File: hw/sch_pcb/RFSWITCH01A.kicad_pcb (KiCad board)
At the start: 2 copper layers, 40.1 x 40.1 mm, 45 parts, among them J1 HEADER_2x03_PARALLEL, J10 HEADER_2x01_PARALLEL, J2 SMA, J3 SMA, J4 HEADER_2x01_PARALLEL, J5 HEADER_2x01_PARALLEL, J6 HEADER_2x01_PARALLEL, J7 SMA, J8 SMA, J9 HEADER_2x01_PARALLEL, M1 HOLE, M2 HOLE, M3 HOLE, M4 HOLE, U1 TPS22945DCKR, U2 PE4259, U3 SPF5189Z, U4 PE4259

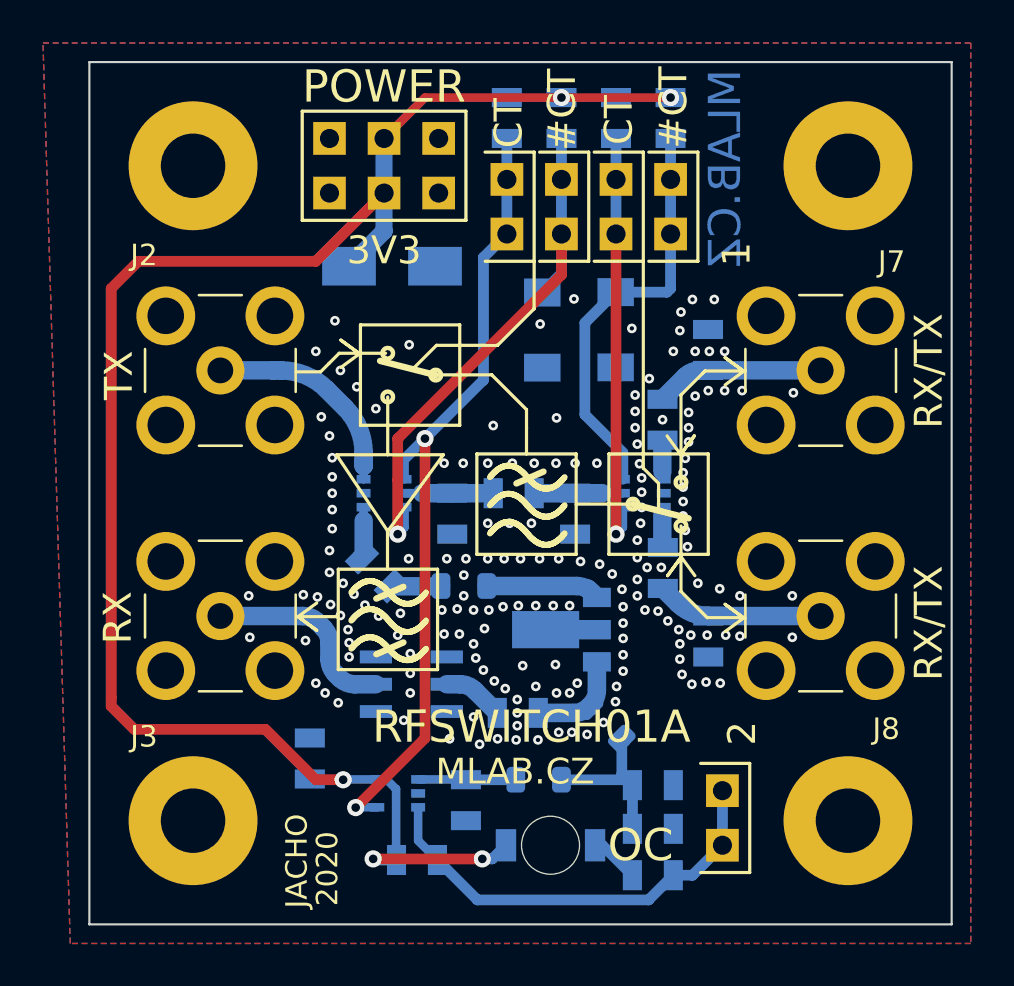
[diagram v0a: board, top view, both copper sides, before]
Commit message: Add shielding vias.
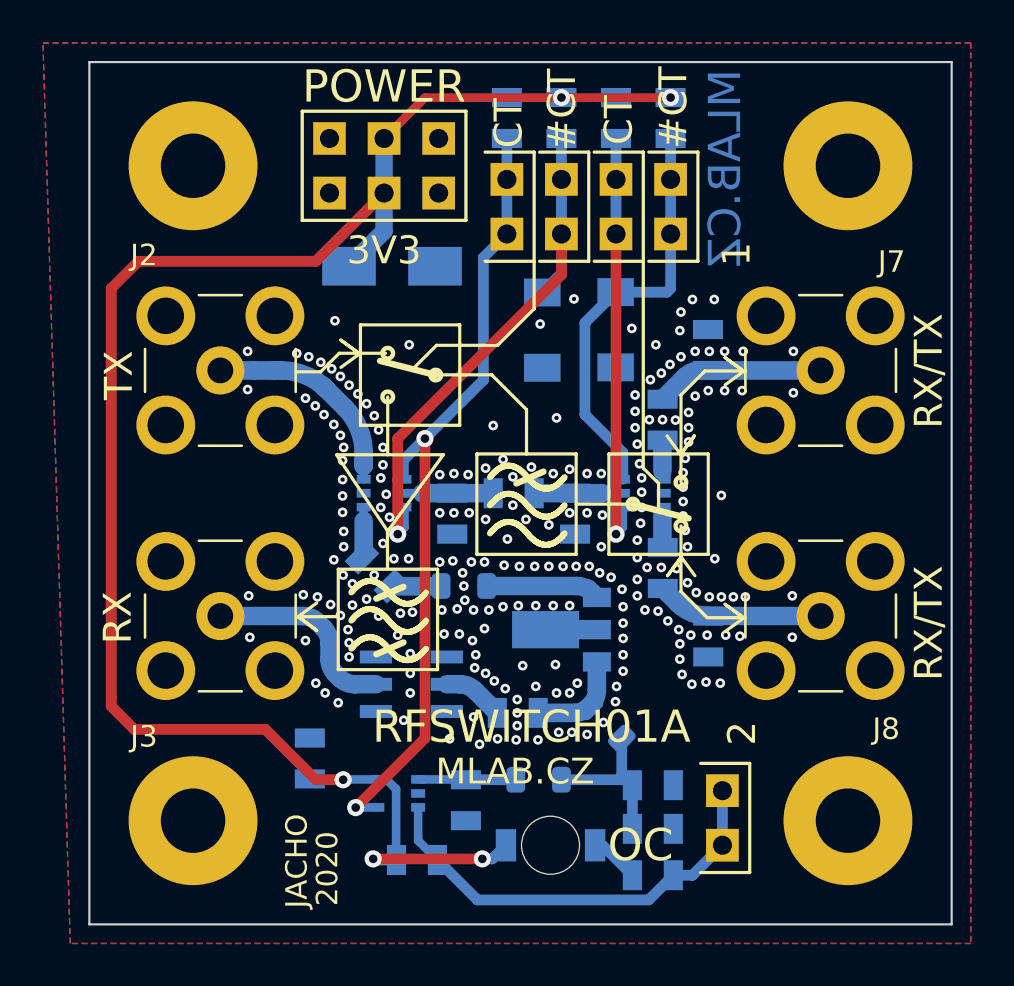
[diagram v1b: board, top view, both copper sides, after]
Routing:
- net GND: vias 170 -> 222
- net /SW1_#CTRL: vias 1 -> 2

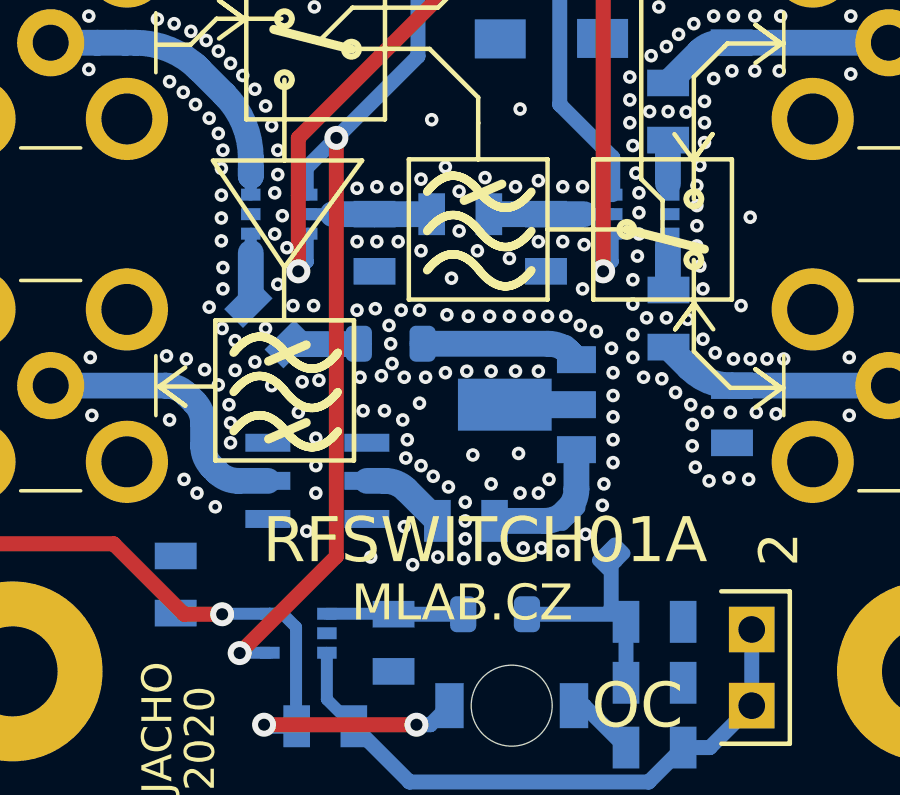
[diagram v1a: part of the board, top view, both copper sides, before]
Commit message: Fix DRC errors.
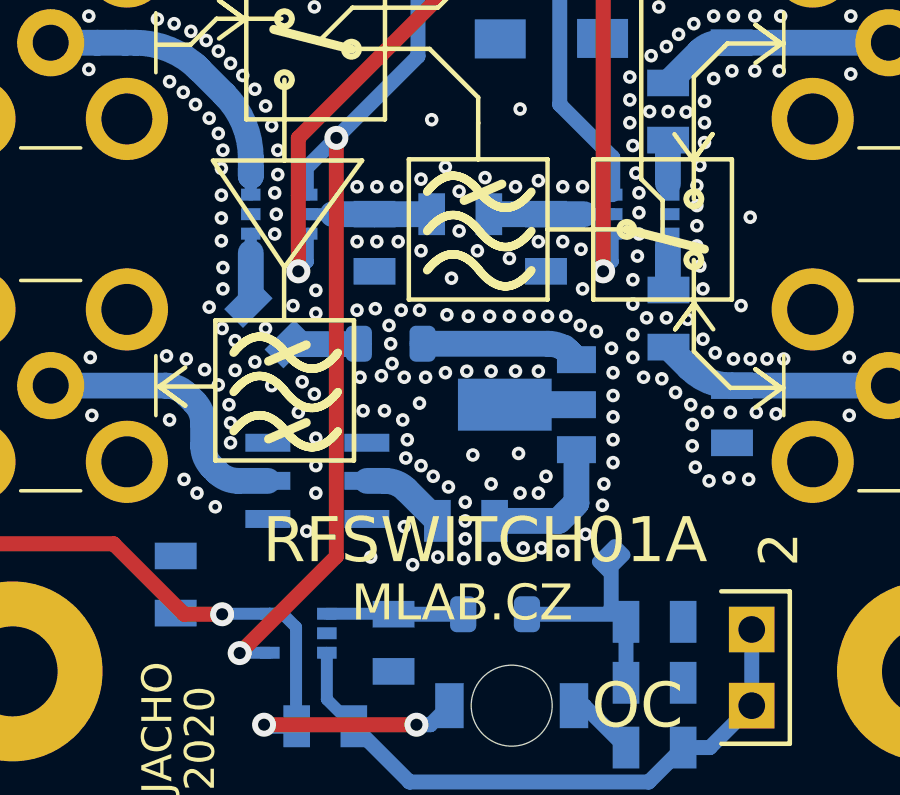
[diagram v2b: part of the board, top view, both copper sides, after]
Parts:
- moved L2 0.05 mm to (24.3, -9.60)
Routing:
- net /SW1_#CTRL: vias 2 -> 1
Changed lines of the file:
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@@
       (viasonmask false)
       (mode 1)
-      (useauxorigin false)
+      (useauxorigin true)
       (hpglpennumber 1)
       (hpglpenspeed 20)
@@
   )
   (module "Inductor_SMD:L_0805_2012Metric" (layer "B.Cu")
-    (at 24.2824 -9.652 135)
+    (at 24.2824 -9.598492 135)
     (descr "Inductor SMD 0805 (2012 Metric), square (rectangular) end terminal, IPC_7351 nominal, (Body size source: IPC-SM-782 page 80, https://www.pcb-3d.com/wordpress/wp-content/uploads/ipc-sm-782a_amendment_1_and_2.pdf), generated with kicad-footprint-generator")
     (tags "inductor")
@@
   (segment (start 13.97 -32.516027) (end 12.3383 -30.884327) (width 0.8) (layer "B.Cu") (net 1))
   (via (at 21.9964 -23.8252) (size 0.45) (drill 0.2) (layers "F.Cu" "B.Cu") (net 2))
-  (via (at 13.9192 -17.9832) (size 0.45) (drill 0.2) (layers "F.Cu" "B.Cu") (net 2))
+  (via (at 15.1892 -17.78) (size 0.45) (drill 0.2) (layers "F.Cu" "B.Cu") (net 2))
   (via (at 25.7556 -18.1356) (size 0.45) (drill 0.2) (layers "F.Cu" "B.Cu") (net 2))
   (via (at 28.2448 -13.716) (size 0.45) (drill 0.2) (layers "F.Cu" "B.Cu") (net 2))
   (via (at 20.1676 -10.0965) (size 0.45) (drill 0.2) (layers "F.Cu" "B.Cu") (net 2))
-  (via (at 15.2908 -14.7828) (size 0.45) (drill 0.2) (layers "F.Cu" "B.Cu") (net 2))
+  (via (at 15.1384 -14.3256) (size 0.45) (drill 0.2) (layers "F.Cu" "B.Cu") (net 2))
   (via (at 23.4188 -21.2344) (size 0.45) (drill 0.2) (layers "F.Cu" "B.Cu") (net 2))
   (via (at 13.8176 -21.0312) (size 0.45) (drill 0.2) (layers "F.Cu" "B.Cu") (net 2))
@@
   (via (at 28.956 -11.5316) (size 0.45) (drill 0.2) (layers "F.Cu" "B.Cu") (net 2))
   (via (at 18.1864 -12.192) (size 0.45) (drill 0.2) (layers "F.Cu" "B.Cu") (net 2))
-  (via (at 24.13 -19.304) (size 0.45) (drill 0.2) (layers "F.Cu" "B.Cu") (net 2))
+  (via (at 24.0284 -19.1516) (size 0.45) (drill 0.2) (layers "F.Cu" "B.Cu") (net 2))
   (via (at 29.1084 -15.494) (size 0.45) (drill 0.2) (layers "F.Cu" "B.Cu") (net 2))
   (via (at 26.929992 -23.741671) (size 0.45) (drill 0.2) (layers "F.Cu" "B.Cu") (net 2))
@@
   (via (at 28.0924 -17.8308) (size 0.45) (drill 0.2) (layers "F.Cu" "B.Cu") (net 2))
   (via (at 19.5072 -21.8948) (size 0.45) (drill 0.2) (layers "F.Cu" "B.Cu") (net 2))
-  (via (at 15.113 -17.272) (size 0.45) (drill 0.2) (layers "F.Cu" "B.Cu") (net 2))
+  (via (at 15.1892 -17.018) (size 0.45) (drill 0.2) (layers "F.Cu" "B.Cu") (net 2))
   (via (at 12.0904 -22.4536) (size 0.45) (drill 0.2) (layers "F.Cu" "B.Cu") (net 2))
   (via (at 27.7368 -27.8892) (size 0.45) (drill 0.2) (layers "F.Cu" "B.Cu") (net 2))
@@
   (via (at 17.1704 -17.1704) (size 0.45) (drill 0.2) (layers "F.Cu" "B.Cu") (net 2))
   (via (at 18.6944 -19.1008) (size 0.45) (drill 0.2) (layers "F.Cu" "B.Cu") (net 2))
-  (via (at 14.0716 -20.2692) (size 0.45) (drill 0.2) (layers "F.Cu" "B.Cu") (net 2))
+  (via (at 13.8684 -20.32) (size 0.45) (drill 0.2) (layers "F.Cu" "B.Cu") (net 2))
   (via (at 11.4808 -15.1384) (size 0.45) (drill 0.2) (layers "F.Cu" "B.Cu") (net 2))
   (via (at 28.1432 -23.368) (size 0.45) (drill 0.2) (layers "F.Cu" "B.Cu") (net 2))
@@
   (via (at 25.9588 -19.6596) (size 0.45) (drill 0.2) (layers "F.Cu" "B.Cu") (net 2))
   (via (at 27.7368 -12.5984) (size 0.45) (drill 0.2) (layers "F.Cu" "B.Cu") (net 2))
-  (via (at 16.5608 -21.1836) (size 0.45) (drill 0.2) (layers "F.Cu" "B.Cu") (net 2))
+  (via (at 16.5608 -21.2344) (size 0.45) (drill 0.2) (layers "F.Cu" "B.Cu") (net 2))
   (via (at 14.4272 -17.272) (size 0.45) (drill 0.2) (layers "F.Cu" "B.Cu") (net 2))
   (via (at 15.1892 -11.938) (size 0.45) (drill 0.2) (layers "F.Cu" "B.Cu") (net 2))
@@
   (via (at 29.6672 -20.2184) (size 0.45) (drill 0.2) (layers "F.Cu" "B.Cu") (net 2))
   (via (at 12.7508 -24.9428) (size 0.45) (drill 0.2) (layers "F.Cu" "B.Cu") (net 2))
-  (via (at 17.8816 -21.1836) (size 0.45) (drill 0.2) (layers "F.Cu" "B.Cu") (net 2))
+  (via (at 17.8816 -21.2344) (size 0.45) (drill 0.2) (layers "F.Cu" "B.Cu") (net 2))
   (via (at 27.2796 -26.3144) (size 0.45) (drill 0.2) (layers "F.Cu" "B.Cu") (net 2))
   (via (at 13.5128 -16.51) (size 0.45) (drill 0.2) (layers "F.Cu" "B.Cu") (net 2))
@@
   (via (at 14.605 -13.716) (size 0.45) (drill 0.2) (layers "F.Cu" "B.Cu") (net 2))
   (via (at 26.3652 -25.6032) (size 0.45) (drill 0.2) (layers "F.Cu" "B.Cu") (net 2))
-  (via (at 22.9616 -11.4808) (size 0.45) (drill 0.2) (layers "F.Cu" "B.Cu") (net 2))
+  (via (at 22.86 -11.5824) (size 0.45) (drill 0.2) (layers "F.Cu" "B.Cu") (net 2))
   (via (at 28.1432 -24.0792) (size 0.45) (drill 0.2) (layers "F.Cu" "B.Cu") (net 2))
   (segment (start 20.1 -6.985) (end 17.78 -6.985) (width 0.5) (layer "B.Cu") (net 3))
   (segment (start 15.555 -7) (end 17.765 -7) (width 0.4) (layer "B.Cu") (net 3))
   (segment (start 17.765 -7) (end 17.78 -6.985) (width 0.4) (layer "B.Cu") (net 3))
-  (segment (start 25.033701 -8.900699) (end 25.033701 -7.224299) (width 0.5) (layer "B.Cu") (net 4))
+  (segment (start 25.033701 -7.224299) (end 25.527 -6.731) (width 0.5) (layer "B.Cu") (net 4))
+  (segment (start 25.1714 -8.763) (end 25.087209 -8.847191) (width 0.5) (layer "B.Cu") (net 4))
   (segment (start 25.527 -4.699) (end 25.527 -6.731) (width 0.5) (layer "B.Cu") (net 4))
-  (segment (start 25.1714 -8.763) (end 25.033701 -8.900699) (width 0.5) (layer "B.Cu") (net 4))
-  (segment (start 25.033701 -7.224299) (end 25.527 -6.731) (width 0.5) (layer "B.Cu") (net 4))
   (segment (start 22.225 -6.985) (end 25.273 -6.985) (width 0.5) (layer "B.Cu") (net 4))
+  (segment (start 25.033701 -8.847191) (end 25.033701 -7.224299) (width 0.5) (layer "B.Cu") (net 4))
   (segment (start 25.273 -6.985) (end 25.527 -6.731) (width 0.5) (layer "B.Cu") (net 4))
+  (segment (start 25.087209 -8.847191) (end 25.033701 -8.847191) (width 0.5) (layer "B.Cu") (net 4))
   (segment (start 18.199893 -11.137107) (end 19.2405 -10.0965) (width 0.861) (layer "B.Cu") (net 5))
   (segment (start 16.89 -11.43) (end 17.492786 -11.43) (width 0.861) (layer "B.Cu") (net 5))
   (arc (start 18.199893 -11.137107) (mid 17.87547 -11.35388) (end 17.492786 -11.43) (width 0.861) (layer "B.Cu") (net 5))
-  (segment (start 23.582107 -10.454309) (end 23.531099 -10.403301) (width 0.861) (layer "B.Cu") (net 6))
-  (segment (start 23.875 -12.47) (end 23.875 -11.161416) (width 0.861) (layer "B.Cu") (net 6))
-  (segment (start 23.517191 -10.389393) (end 23.531099 -10.403301) (width 0.861) (layer "B.Cu") (net 6))
-  (segment (start 21.1455 -10.0965) (end 22.810084 -10.0965) (width 0.861) (layer "B.Cu") (net 6))
-  (arc (start 23.582107 -10.454309) (mid 23.79888 -10.778732) (end 23.875 -11.161416) (width 0.861) (layer "B.Cu") (net 6))
-  (arc (start 22.810084 -10.0965) (mid 23.192767 -10.17262) (end 23.517191 -10.389393) (width 0.861) (layer "B.Cu") (net 6))
+  (segment (start 23.875 -12.47) (end 23.875 -10.693694) (width 0.861) (layer "B.Cu") (net 6))
+  (segment (start 21.1455 -10.0965) (end 23.277806 -10.0965) (width 0.861) (layer "B.Cu") (net 6))
+  (segment (start 23.875 -10.693694) (end 23.531099 -10.349793) (width 0.861) (layer "B.Cu") (net 6))
+  (segment (start 23.277806 -10.0965) (end 23.531099 -10.349793) (width 0.861) (layer "B.Cu") (net 6))
   (segment (start 26.924 -22.783179) (end 26.924 -21.336) (width 0.861) (layer "B.Cu") (net 7))
   (segment (start 26.929992 -22.789171) (end 26.924 -22.783179) (width 0.861) (layer "B.Cu") (net 7))
@@
   (segment (start 14.605 -22.86) (end 14.605 -20.955) (width 0.5) (layer "F.Cu") (net 13))
   (segment (start 14.605 -20.955) (end 14.605 -18.415) (width 0.5) (layer "F.Cu") (net 13))
-  (via (at 14.224 -19.2024) (size 0.45) (drill 0.2) (layers "F.Cu" "B.Cu") (net 13))
   (via (at 14.605 -18.415) (size 0.8) (drill 0.4) (layers "F.Cu" "B.Cu") (net 13))
   (segment (start 14.92 -18.73) (end 14.605 -18.415) (width 0.4) (layer "B.Cu") (net 13))

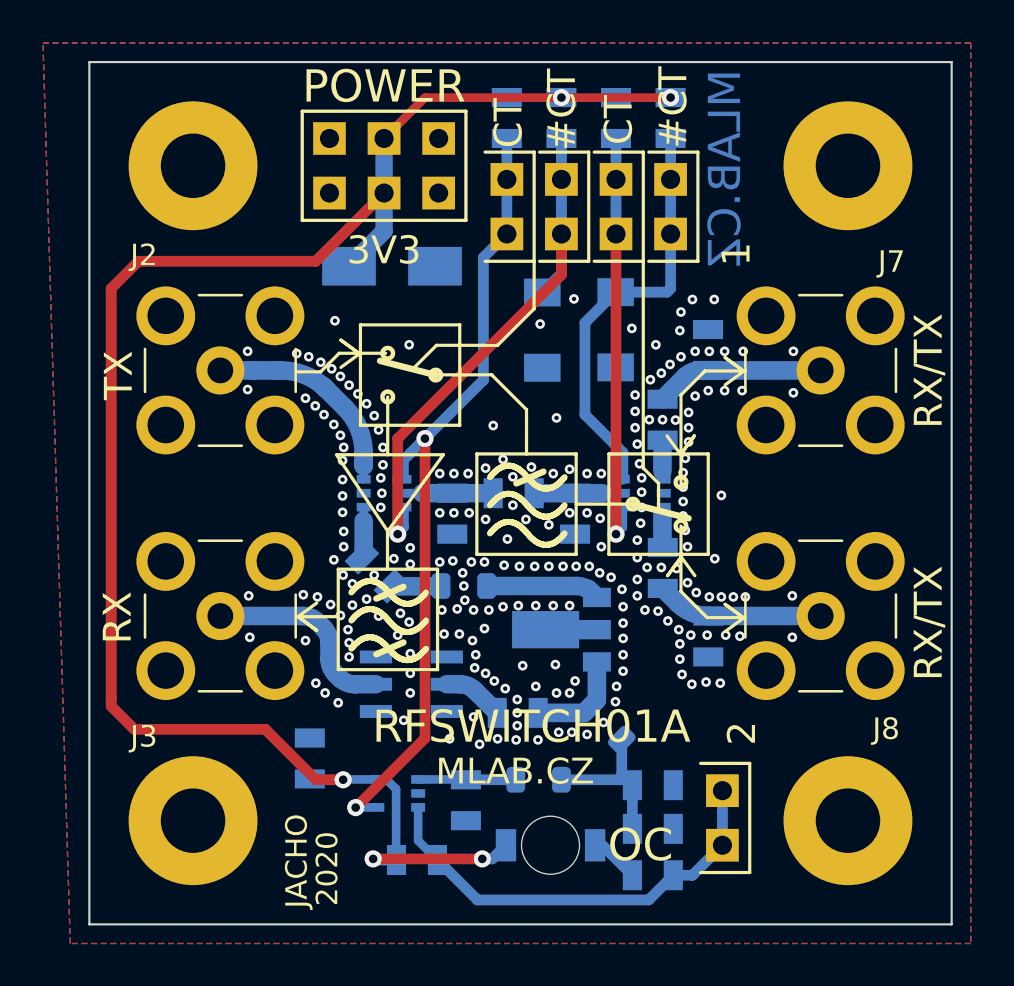
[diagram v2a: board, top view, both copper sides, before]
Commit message: Cleanup vias in silksceen.
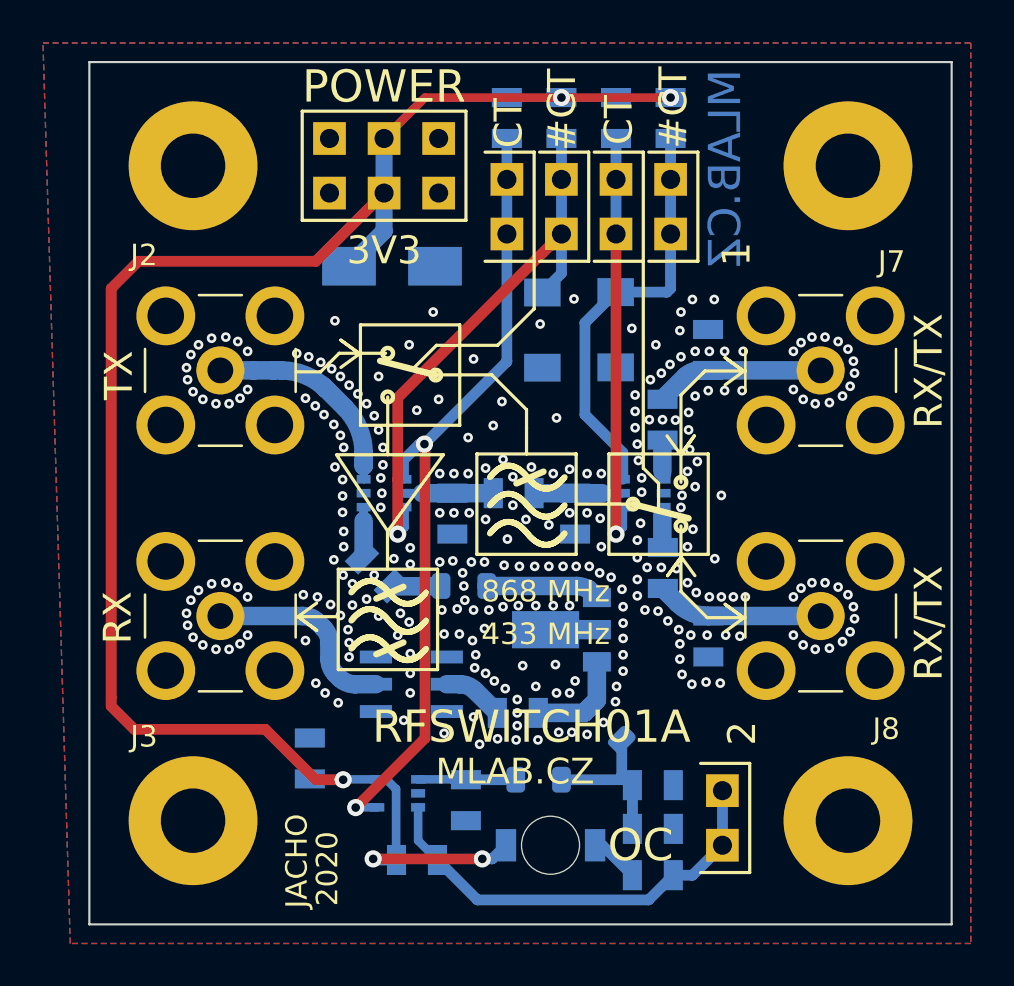
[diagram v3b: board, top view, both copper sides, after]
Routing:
- net GND: vias 222 -> 276
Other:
- board text added: "433 MHz"
- board text added: "868 MHz"
